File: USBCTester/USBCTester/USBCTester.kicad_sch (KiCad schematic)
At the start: 67 parts, among them J1 AUSB1-DFN-PTR3, J2 AUSB1-DFN-PTR3, J4 Conn_01x03, J5 Conn_01x08, J6 Conn_01x03, SW1 SW_Push, U1 74HC595, U2 74HC595, U3 74HC595, U4 74HC595, U5 74HC595, U6 74HC595, U7 RaspberryPi_Pico

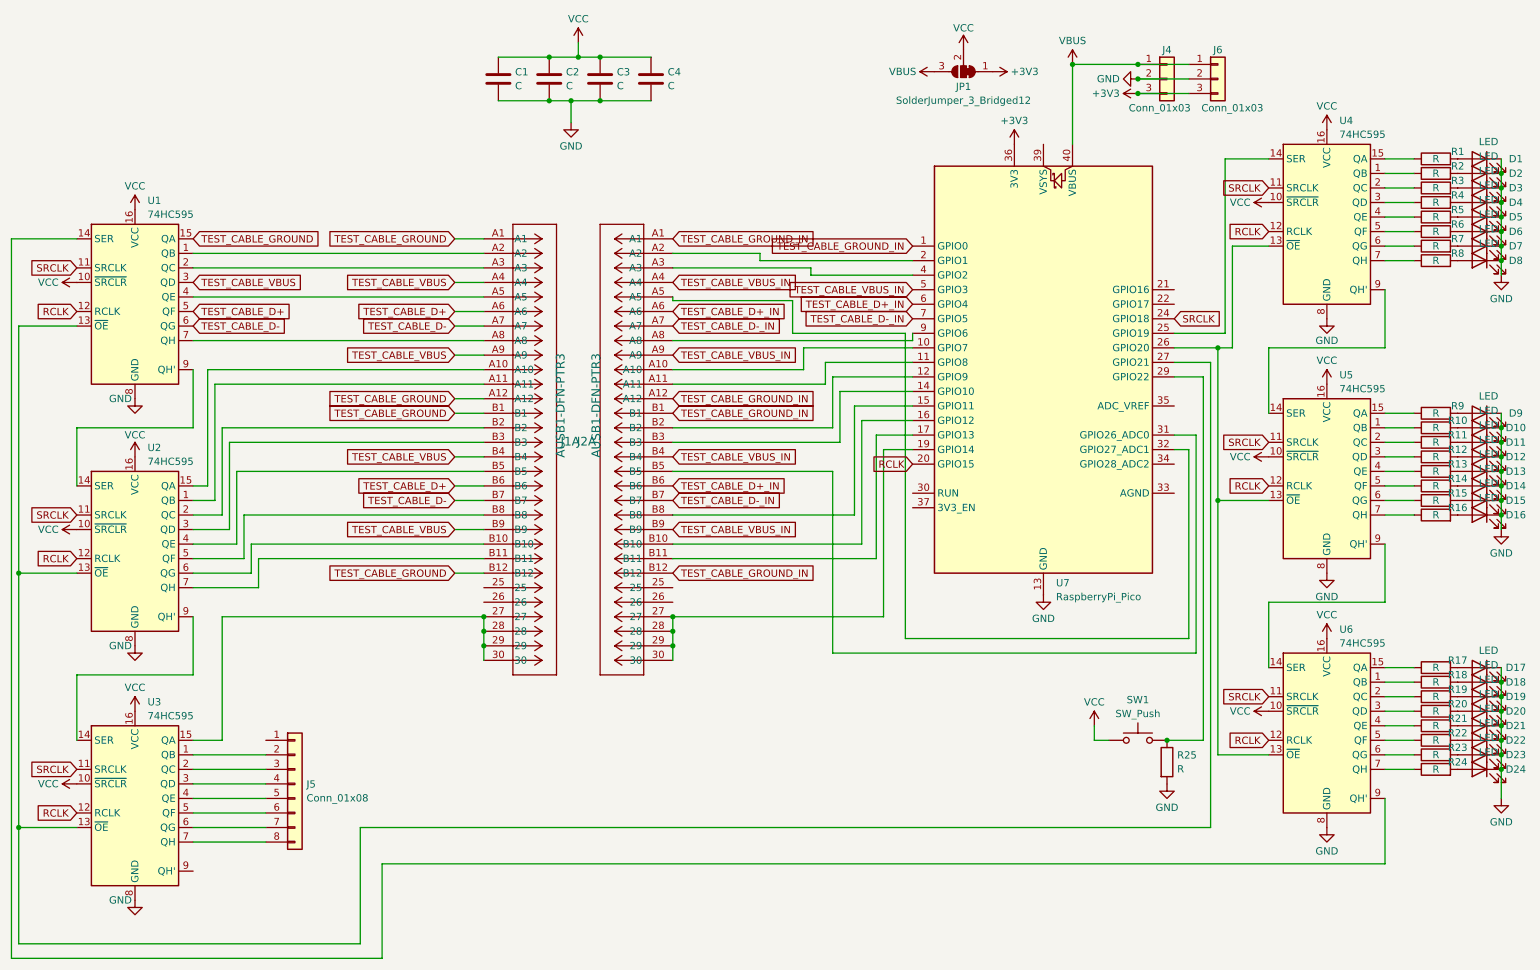
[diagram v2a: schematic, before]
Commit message: add more leds and route almost everything
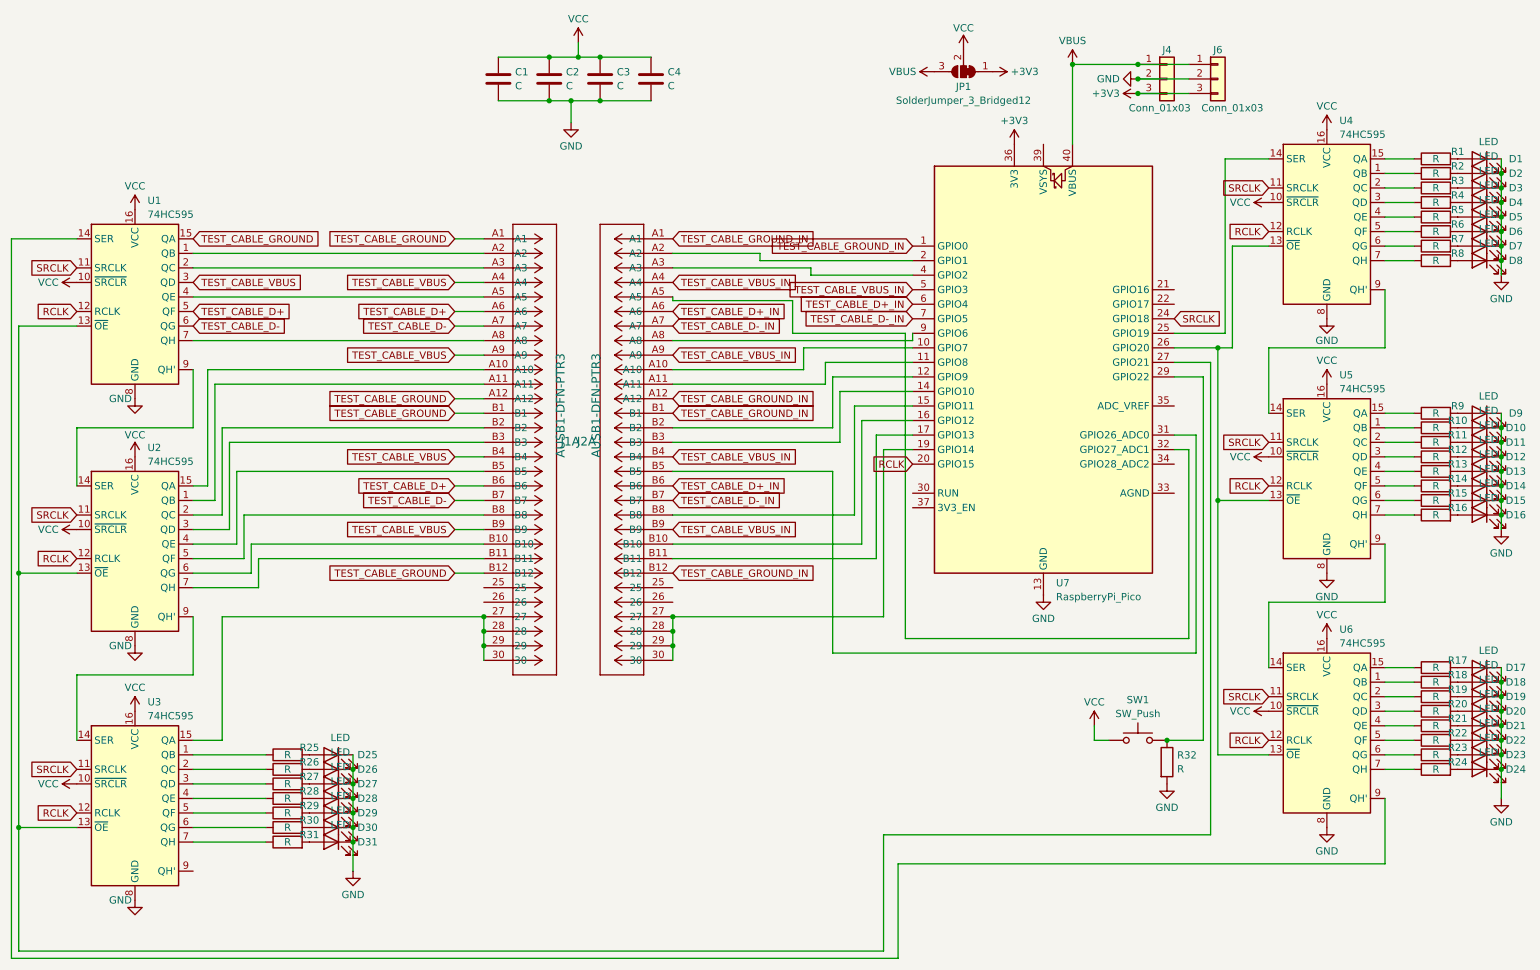
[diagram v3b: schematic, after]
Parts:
- removed J5: Conn_01x08, symbol Connector_Generic:Conn_01x08
- added D25, D26, D27, D28, D29, D30, D31: LED, LED_SMD:LED_0603_1608Metric, symbol Device:LED
- added R26, R27, R28, R29, R30, R31, R32: R, Resistor_SMD:R_0603_1608Metric, symbol Device:R
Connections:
- net GND: now also D25.1 (K), D26.1 (K), D27.1 (K), D28.1 (K), D29.1 (K), D30.1 (K), D31.1 (K), R32.2; no longer R25.2
- net at SW1.2, U7.29 (GPIO22): now also R32.1; no longer R25.1
- net at U3.1 (QB): now also R25.1
- net at U3.2 (QC): now also R26.1
- net at U3.3 (QD): now also R27.1
- net at U3.4 (QE): now also R28.1
- net at U3.5 (QF): now also R29.1
- net at U3.6 (QG): now also R30.1
- net at U3.7 (QH): now also R31.1
- new net: D30.2 (A), R30.2
- new net: D26.2 (A), R26.2
- new net: D27.2 (A), R27.2
- new net: D28.2 (A), R28.2
- new net: D31.2 (A), R31.2
- new net: D29.2 (A), R29.2
- new net: D25.2 (A), R25.2

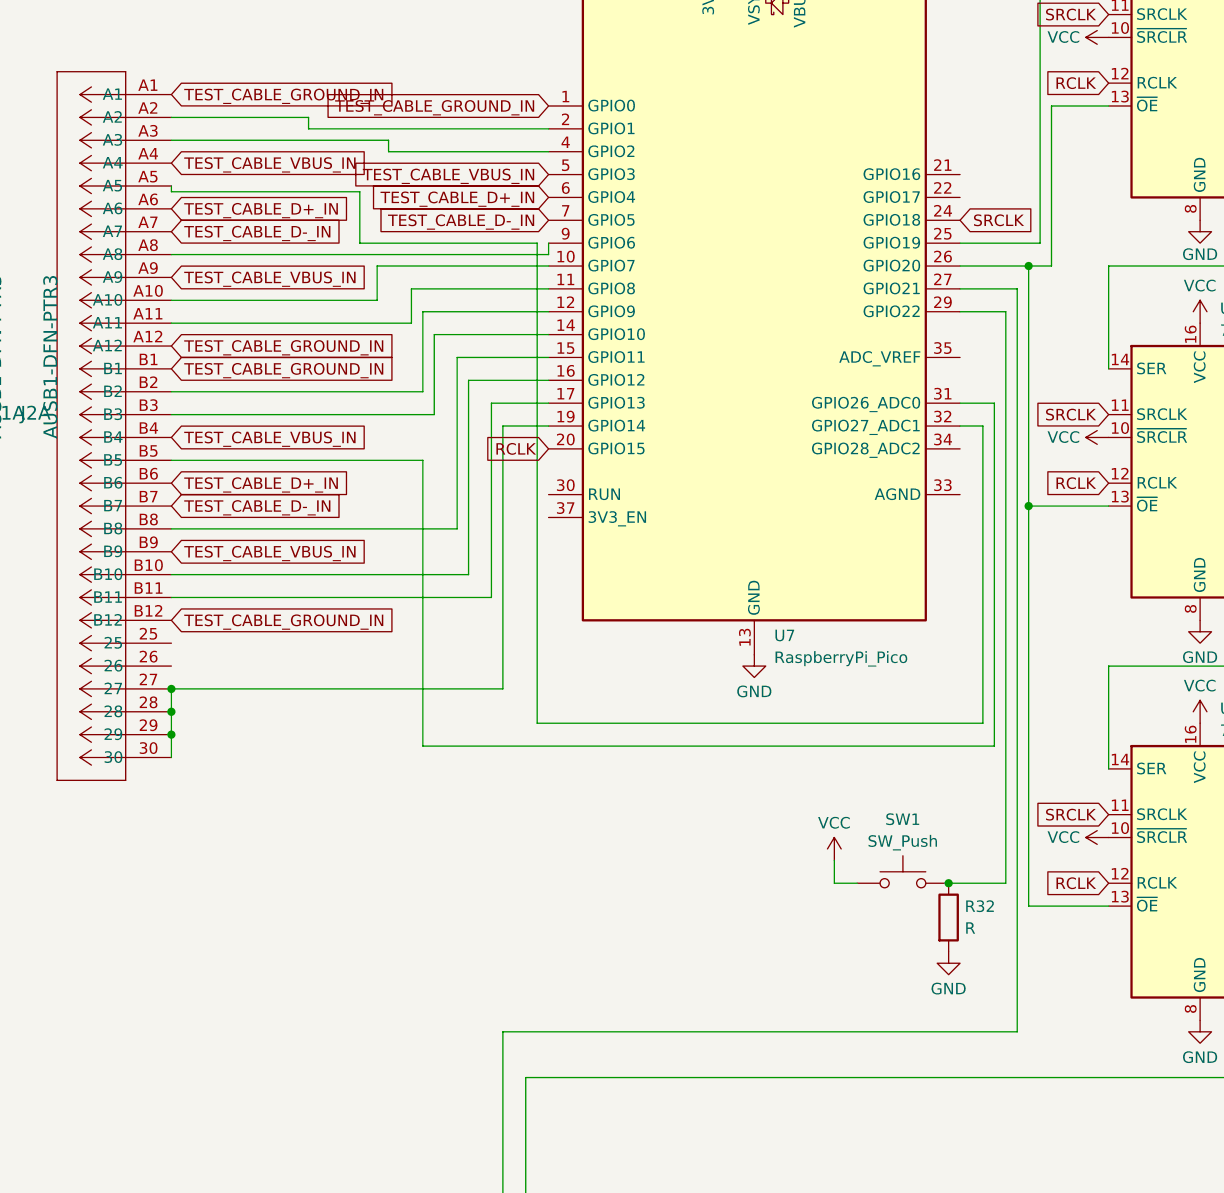
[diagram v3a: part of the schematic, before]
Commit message: add breakout pins for prototyping
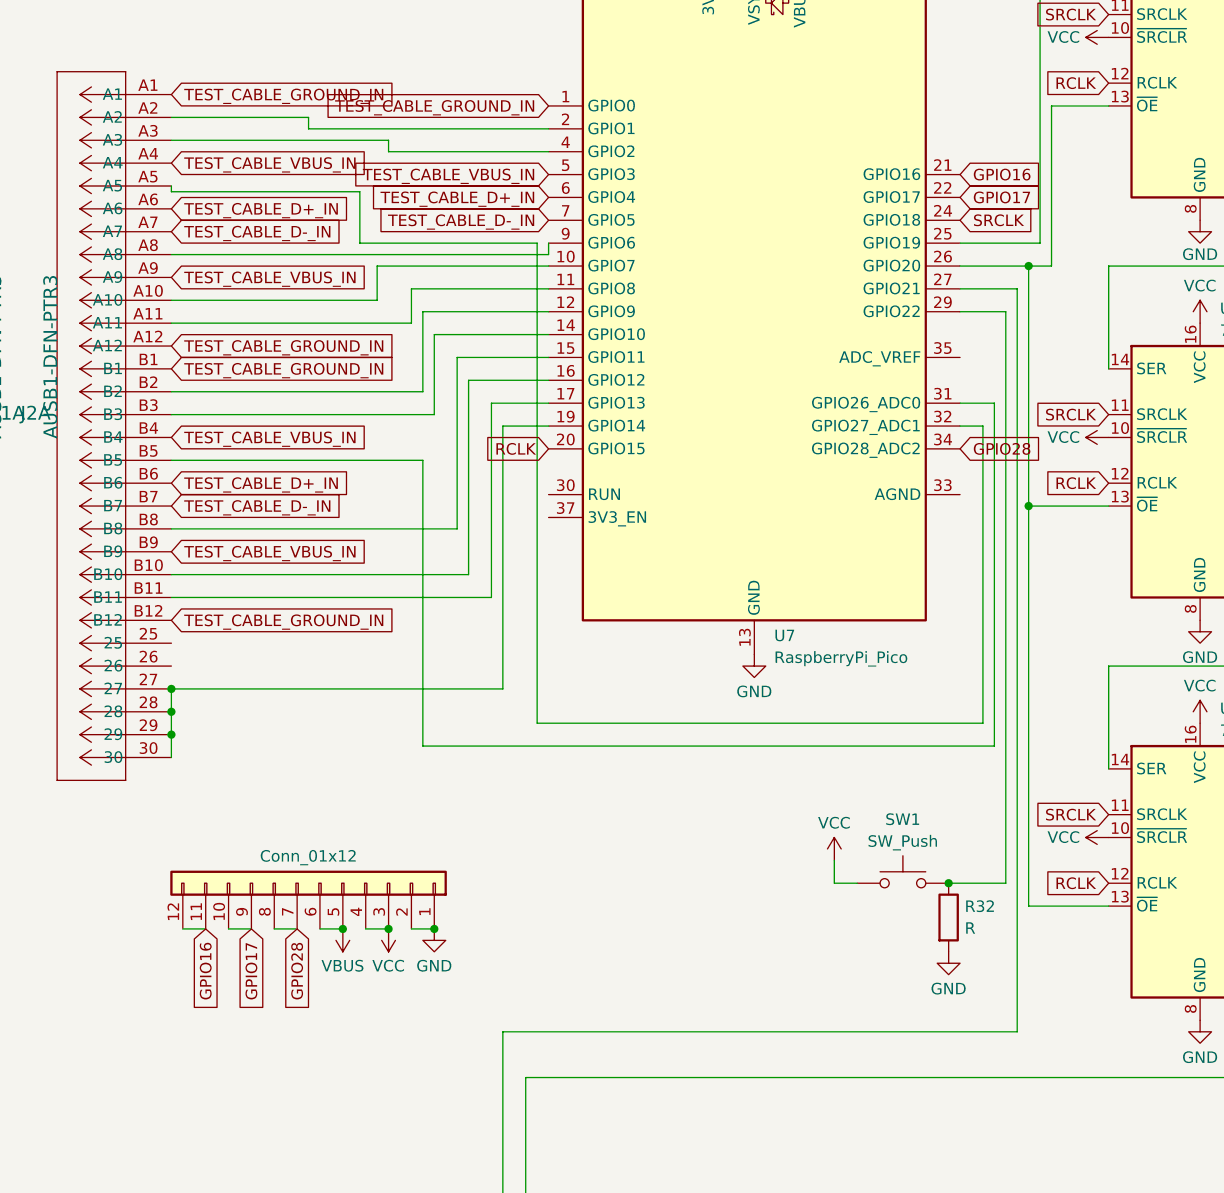
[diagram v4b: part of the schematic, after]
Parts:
- added J3: Conn_01x12, Connector_PinSocket_2.54mm:PinSocket_1x12_P2.54mm_Vertical, symbol Connector_Generic:Conn_01x12
- J4, J6: footprint (none) -> Connector_PinSocket_2.54mm:PinSocket_1x03_P2.54mm_Vertical
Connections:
- net GND: now also J3.1 (Pin_1), J3.2 (Pin_2)
- net VBUS: now also J3.5 (Pin_5), J3.6 (Pin_6)
- net VCC: now also J3.3 (Pin_3), J3.4 (Pin_4)
- net GPIO16: now reaches U7.21 (GPIO16)
- net GPIO16: now also J3.11 (Pin_11), J3.12 (Pin_12)
- net GPIO17: now reaches U7.22 (GPIO17)
- net GPIO17: now also J3.10 (Pin_10), J3.9 (Pin_9)
- net GPIO28: now reaches U7.34 (GPIO28_ADC2)
- net GPIO28: now also J3.7 (Pin_7), J3.8 (Pin_8)
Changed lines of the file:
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@@
   (junction (at 113.03 30.48) (diameter 0) (color 0 0 0 0)
   )
+  (junction (at 158.75 147.32) (diameter 0) (color 0 0 0 0)
+  )
   (junction (at 229.87 73.66) (diameter 0) (color 0 0 0 0)
   )
   (junction (at 279.4 137.16) (diameter 0) (color 0 0 0 0)
   )
+  (junction (at 163.83 147.32) (diameter 0) (color 0 0 0 0)
+  )
   (junction (at 134.62 123.19) (diameter 0) (color 0 0 0 0)
   )
@@
   (junction (at 121.92 22.86) (diameter 0) (color 0 0 0 0)
   )
+  (junction (at 153.67 147.32) (diameter 0) (color 0 0 0 0)
+  )
   (junction (at 279.4 142.24) (diameter 0) (color 0 0 0 0)
   )
@@
     (stroke (width 0) (type default))
   )
+  (wire (pts (xy 140.97 147.32) (xy 143.51 147.32))
+    (stroke (width 0) (type default))
+  )
   (wire (pts (xy 175.26 124.46) (xy 224.79 124.46))
     (stroke (width 0) (type default))
@@
     (stroke (width 0) (type default))
   )
+  (wire (pts (xy 161.29 147.32) (xy 163.83 147.32))
+    (stroke (width 0) (type default))
+  )
   (wire (pts (xy 158.75 59.69) (xy 158.75 60.96))
     (stroke (width 0) (type default))
@@
     (stroke (width 0) (type default))
   )
+  (wire (pts (xy 135.89 147.32) (xy 138.43 147.32))
+    (stroke (width 0) (type default))
+  )
   (wire (pts (xy 163.83 81.28) (xy 163.83 90.17))
     (stroke (width 0) (type default))
@@
     (stroke (width 0) (type default))
   )
+  (wire (pts (xy 151.13 147.32) (xy 153.67 147.32))
+    (stroke (width 0) (type default))
+  )
   (wire (pts (xy 279.4 100.33) (xy 279.4 102.87))
     (stroke (width 0) (type default))
@@
     (stroke (width 0) (type default))
   )
+  (wire (pts (xy 146.05 147.32) (xy 148.59 147.32))
+    (stroke (width 0) (type default))
+  )
   (wire (pts (xy 134.62 125.73) (xy 134.62 128.27))
     (stroke (width 0) (type default))
@@
     (stroke (width 0) (type default))
   )
+  (wire (pts (xy 156.21 147.32) (xy 158.75 147.32))
+    (stroke (width 0) (type default))
+  )
   (wire (pts (xy 78.74 160.02) (xy 78.74 165.1))
     (stroke (width 0) (type default))
@@
     )
   )
+  (global_label "GPIO16" (shape input) (at 138.43 147.32 270) (fields_autoplaced)
+    (effects (font (size 1.27 1.27)) (justify right))
+    (property "Intersheetrefs" "${INTERSHEET_REFS}" (at 138.43 157.1995 90)
+      (effects (font (size 1.27 1.27)) (justify right) hide)
+    )
+  )
   (global_label "SRCLK" (shape input) (at 30.48 102.87 180) (fields_autoplaced)
     (effects (font (size 1.27 1.27)) (justify right))
@@
     )
   )
+  (global_label "GPIO16" (shape input) (at 222.25 63.5 0) (fields_autoplaced)
+    (effects (font (size 1.27 1.27)) (justify left))
+    (property "Intersheetrefs" "${INTERSHEET_REFS}" (at 232.1295 63.5 0)
+      (effects (font (size 1.27 1.27)) (justify left) hide)
+    )
+  )
   (global_label "TEST_CABLE_GROUND" (shape input) (at 96.52 113.03 180) (fields_autoplaced)
     (effects (font (size 1.27 1.27)) (justify right))
@@
     )
   )
+  (global_label "GPIO28" (shape input) (at 148.59 147.32 270) (fields_autoplaced)
+    (effects (font (size 1.27 1.27)) (justify right))
+    (property "Intersheetrefs" "${INTERSHEET_REFS}" (at 148.59 157.1995 90)
+      (effects (font (size 1.27 1.27)) (justify right) hide)
+    )
+  )
   (global_label "RCLK" (shape input) (at 176.53 93.98 180) (fields_autoplaced)
     (effects (font (size 1.27 1.27)) (justify right))
@@
     )
   )
+  (global_label "GPIO17" (shape input) (at 143.51 147.32 270) (fields_autoplaced)
+    (effects (font (size 1.27 1.27)) (justify right))
+    (property "Intersheetrefs" "${INTERSHEET_REFS}" (at 143.51 157.1995 90)
+      (effects (font (size 1.27 1.27)) (justify right) hide)
+    )
+  )
   (global_label "TEST_CABLE_VBUS" (shape input) (at 96.52 62.23 180) (fields_autoplaced)
     (effects (font (size 1.27 1.27)) (justify right))
@@
     )
   )
+  (global_label "GPIO28" (shape input) (at 222.25 93.98 0) (fields_autoplaced)
+    (effects (font (size 1.27 1.27)) (justify left))
+    (property "Intersheetrefs" "${INTERSHEET_REFS}" (at 232.1295 93.98 0)
+      (effects (font (size 1.27 1.27)) (justify left) hide)
+    )
+  )
   (global_label "TEST_CABLE_D+_IN" (shape input) (at 134.62 97.79 0) (fields_autoplaced)
     (effects (font (size 1.27 1.27)) (justify left))
@@
     )
   )
+  (global_label "GPIO17" (shape input) (at 222.25 66.04 0) (fields_autoplaced)
+    (effects (font (size 1.27 1.27)) (justify left))
+    (property "Intersheetrefs" "${INTERSHEET_REFS}" (at 232.1295 66.04 0)
+      (effects (font (size 1.27 1.27)) (justify left) hide)
+    )
+  )
   (global_label "TEST_CABLE_GROUND_IN" (shape input) (at 134.62 85.09 0) (fields_autoplaced)
     (effects (font (size 1.27 1.27)) (justify left))
@@
     )
   )
+  (symbol (lib_id "power:GND") (at 163.83 147.32 0) (unit 1)
+    (in_bom yes) (on_board yes) (dnp no) (fields_autoplaced)
+    (property "Reference" "#PWR020" (at 163.83 153.67 0)
+      (effects (font (size 1.27 1.27)) hide)
+    )
+    (property "Value" "GND" (at 163.83 151.4531 0)
+      (effects (font (size 1.27 1.27)))
+    )
+    (property "Footprint" "" (at 163.83 147.32 0)
+      (effects (font (size 1.27 1.27)) hide)
+    )
+    (property "Datasheet" "" (at 163.83 147.32 0)
+      (effects (font (size 1.27 1.27)) hide)
+    )
+    (pin "1")
+    (instances
+      (project "USBCTester"
+        (path "/8a9ba22b-e32e-4058-9f6d-d23fc913e7b1"
+          (reference "#PWR020") (unit 1)
+        )
+      )
+    )
+  )
   (symbol (lib_id "Device:R") (at 267.97 139.7 90) (unit 1)
     (in_bom yes) (on_board yes) (dnp no)
@@
       (effects (font (size 1.27 1.27)))
     )
-    (property "Footprint" "" (at 220.98 26.67 0)
+    (property "Footprint" "Connector_PinSocket_2.54mm:PinSocket_1x03_P2.54mm_Vertical" (at 220.98 26.67 0)
       (effects (font (size 1.27 1.27)) hide)
     )
@@
     )
   )
+  (symbol (lib_id "power:VCC") (at 158.75 147.32 180) (unit 1)
+    (in_bom yes) (on_board yes) (dnp no) (fields_autoplaced)
+    (property "Reference" "#PWR022" (at 158.75 143.51 0)
+      (effects (font (size 1.27 1.27)) hide)
+    )
+    (property "Value" "VCC" (at 158.75 151.4531 0)
+      (effects (font (size 1.27 1.27)))
+    )
+    (property "Footprint" "" (at 158.75 147.32 0)
+      (effects (font (size 1.27 1.27)) hide)
+    )
+    (property "Datasheet" "" (at 158.75 147.32 0)
+      (effects (font (size 1.27 1.27)) hide)
+    )
+    (pin "1")
+    (instances
+      (project "USBCTester"
+        (path "/8a9ba22b-e32e-4058-9f6d-d23fc913e7b1"
+          (reference "#PWR022") (unit 1)
+        )
+      )
+    )
+  )
   (symbol (lib_id "power:VCC") (at 185.42 21.59 0) (unit 1)
     (in_bom yes) (on_board yes) (dnp no)
@@
     )
   )
+  (symbol (lib_id "power:VBUS") (at 153.67 147.32 180) (unit 1)
+    (in_bom yes) (on_board yes) (dnp no)
+    (property "Reference" "#PWR023" (at 153.67 143.51 0)
+      (effects (font (size 1.27 1.27)) hide)
+    )
+    (property "Value" "VBUS" (at 153.67 151.4531 0)
+      (effects (font (size 1.27 1.27)))
+    )
+    (property "Footprint" "" (at 153.67 147.32 0)
+      (effects (font (size 1.27 1.27)) hide)
+    )
+    (property "Datasheet" "" (at 153.67 147.32 0)
+      (effects (font (size 1.27 1.27)) hide)
+    )
+    (pin "1")
+    (instances
+      (project "USBCTester"
+        (path "/8a9ba22b-e32e-4058-9f6d-d23fc913e7b1"
+          (reference "#PWR023") (unit 1)
+        )
+      )
+    )
+  )
   (symbol (lib_id "Device:LED") (at 74.93 160.02 0) (mirror y) (unit 1)
     (in_bom yes) (on_board yes) (dnp no)
@@
       (effects (font (size 1.27 1.27)))
     )
-    (property "Footprint" "" (at 229.87 26.67 0)
+    (property "Footprint" "Connector_PinSocket_2.54mm:PinSocket_1x03_P2.54mm_Vertical" (at 229.87 26.67 0)
       (effects (font (size 1.27 1.27)) hide)
     )
@@
         )
       )
+    )
+  )
+  (symbol (lib_id "Connector_Generic:Conn_01x12") (at 151.13 142.24 270) (mirror x) (unit 1)
+    (in_bom yes) (on_board yes) (dnp no)
+    (property "Reference" "J3" (at 149.86 136.8257 90)
+      (effects (font (size 1.27 1.27)) hide)
+    )
+    (property "Value" "Conn_01x12" (at 149.86 139.2499 90)
+      (effects (font (size 1.27 1.27)))
+    )
+    (property "Footprint" "Connector_PinSocket_2.54mm:PinSocket_1x12_P2.54mm_Vertical" (at 151.13 142.24 0)
+      (effects (font (size 1.27 1.27)) hide)
+    )
+    (property "Datasheet" "~" (at 151.13 142.24 0)
+      (effects (font (size 1.27 1.27)) hide)
+    )
+    (pin "6")
+    (pin "4")
+    (pin "3")
+    (pin "9")
+    (pin "5")
+    (pin "1")
+    (pin "10")
+    (pin "11")
+    (pin "2")
+    (pin "12")
+    (pin "8")
+    (pin "7")
+    (instances
+      (project "USBCTester"
+        (path "/8a9ba22b-e32e-4058-9f6d-d23fc913e7b1"
+          (reference "J3") (unit 1)
+        )
+      )
